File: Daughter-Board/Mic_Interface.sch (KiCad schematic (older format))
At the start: 11 parts, among them J301 Conn_01x08_0.5mm_Female_Kyoce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, U102 LM324A, U105 74HC4016, U107 MC74VHCT126A, U108 74HC4016

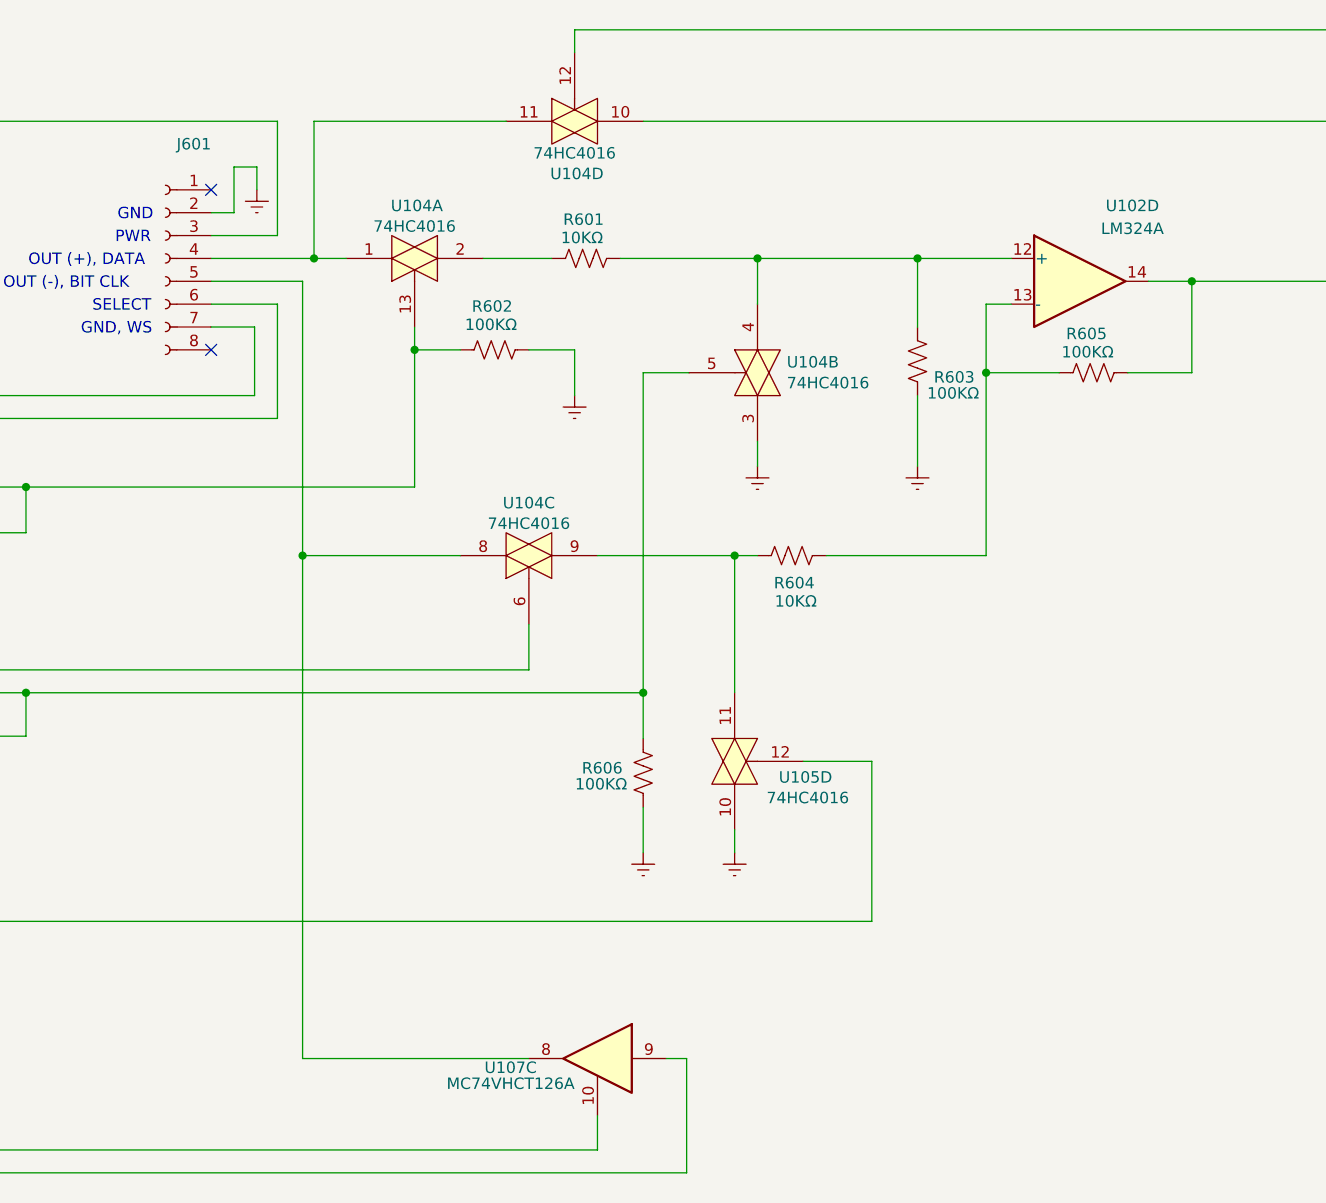
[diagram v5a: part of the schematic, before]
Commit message: Add connector for PICkit to MCU interface.
In the process of adding the PICkit connector some control lines had to be moved.
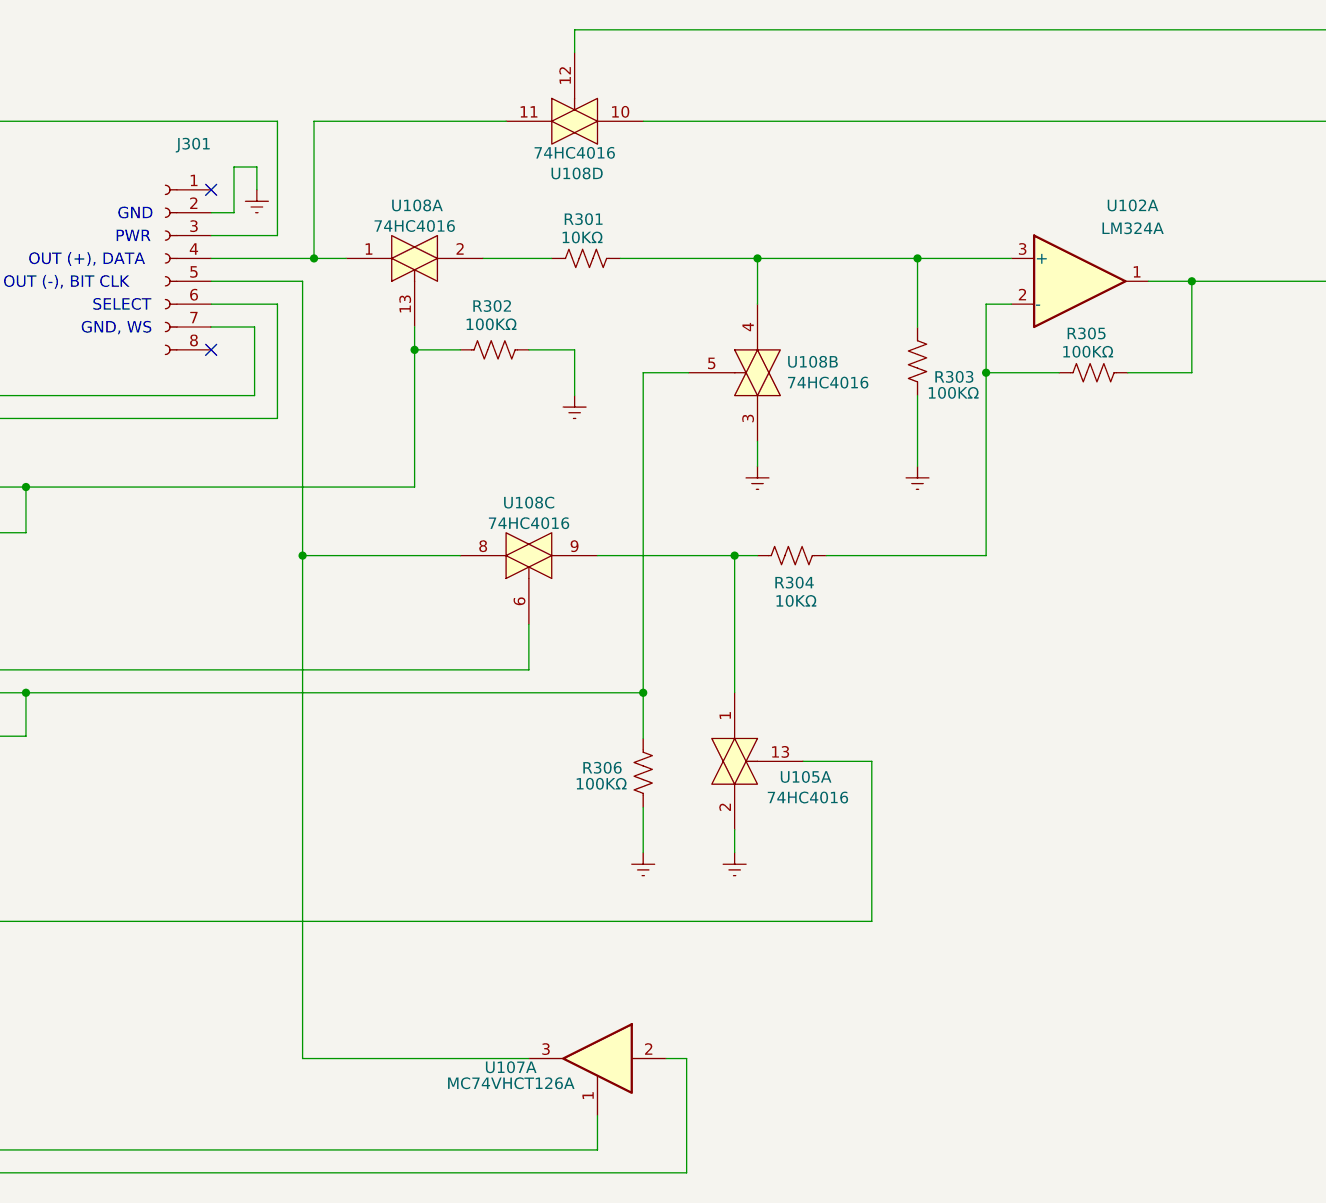
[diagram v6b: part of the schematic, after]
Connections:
- net AOut: now also U102.1; no longer U102.14
- net CLK_EN: now also U107.1; no longer U107.10
- net GNDREF: now also U105.2; no longer U105.10
- net MST_CLK: now also U107.2; no longer U107.9
- net SingleGain: now also U105.13; no longer U105.12
- net at R301.1, R303.2, U108.4: now also U102.3 (+); no longer U102.12 (+)
- net at R304.2, R305.2: now also U102.2 (-); no longer U102.13 (-)
- net at R304.1, U108.9: now also U105.1; no longer U105.11
- net at J301.5 (Pin_5), U108.8: now also U107.3; no longer U107.8
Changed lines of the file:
@@
 $Descr A4 11693 8268
 encoding utf-8
-Sheet 6 6
+Sheet 3 6
 Title "Daughter Board"
 Date ""
@@
 AR Path="/6159E578/612F28D7" Ref="R601"  Part="1"
 AR Path="/6159EF26/612F28D7" Ref="R501"  Part="1"
-F 0 "R601" V 6080 1900 50  0000 L CNN
+F 0 "R301" V 6080 1900 50  0000 L CNN
 F 1 "10KΩ" V 6160 1890 50  0000 L CNN
 F 2 "Resistor_SMD:R_1206_3216Metric" V 6290 1990 50  0001 C CNN
@@
 AR Path="/6159E578/612F28DD" Ref="R603"  Part="1"
 AR Path="/6159EF26/612F28DD" Ref="R503"  Part="1"
-F 0 "R603" H 7450 2520 50  0000 L CNN
+F 0 "R303" H 7450 2520 50  0000 L CNN
 F 1 "100KΩ" H 7430 2590 50  0000 L CNN
 F 2 "Resistor_SMD:R_1206_3216Metric" V 7740 2440 50  0001 C CNN
@@
 $Comp
 L Amplifier_Operational:LM324A U?
-U 4 1 612F28EA
+U 1 1 612F28EA
 P 8410 2100
 AR Path="/612F28EA" Ref="U?"  Part="1"
@@
 F 2 "Package_SO:SOIC-14_3.9x8.7mm_P1.27mm" H 8360 2200 50  0001 C CNN
 F 3 "" H 8460 2300 50  0001 C CNN
-	4    8410 2100
+	1    8410 2100
 	1    0    0    -1
 $EndComp
@@
 AR Path="/6159E578/612F28F6" Ref="R605"  Part="1"
 AR Path="/6159EF26/612F28F6" Ref="R505"  Part="1"
-F 0 "R605" V 8300 2380 50  0000 L CNN
+F 0 "R305" V 8300 2380 50  0000 L CNN
 F 1 "100KΩ" V 8380 2360 50  0000 L CNN
 F 2 "Resistor_SMD:R_1206_3216Metric" V 8510 2490 50  0001 C CNN
@@
 AR Path="/6159E578/612F2915" Ref="R604"  Part="1"
 AR Path="/6159EF26/612F2915" Ref="R504"  Part="1"
-F 0 "R604" V 7030 3200 50  0000 L CNN
+F 0 "R304" V 7030 3200 50  0000 L CNN
 F 1 "10KΩ" V 6950 3190 50  0000 L CNN
 F 2 "Resistor_SMD:R_1206_3216Metric" V 7190 3290 50  0001 C CNN
@@
 $Comp
 L 74xx:74LS126 U?
-U 3 1 612F29C2
+U 1 1 612F29C2
 P 6300 5500
 AR Path="/60E235BF/612F29C2" Ref="U?"  Part="1"
@@
 F 3 "" H 6300 5500 50  0001 C CNN
 F 4 "771-74VHCT126D118" H 6300 5500 50  0001 C CNN "Mouser #"
-	3    6300 5500
+	1    6300 5500
 	-1   0    0    -1
 $EndComp
@@
 AR Path="/6159E578/6151F074" Ref="R606"  Part="1"
 AR Path="/6159EF26/6151F074" Ref="R506"  Part="1"
-F 0 "R606" H 6590 4230 50  0000 L CNN
+F 0 "R306" H 6590 4230 50  0000 L CNN
 F 1 "100KΩ" H 6570 4300 50  0000 L CNN
 F 2 "Resistor_SMD:R_1206_3216Metric" V 6540 4240 50  0001 C CNN
@@
 AR Path="/6159E578/61527AC0" Ref="R602"  Part="1"
 AR Path="/6159EF26/61527AC0" Ref="R502"  Part="1"
-F 0 "R602" V 5660 2300 50  0000 L CNN
+F 0 "R302" V 5660 2300 50  0000 L CNN
 F 1 "100KΩ" V 5740 2270 50  0000 L CNN
 F 2 "Resistor_SMD:R_1206_3216Metric" V 5890 2390 50  0001 C CNN
@@
 AR Path="/6159E578/612F293F" Ref="J601"  Part="1"
 AR Path="/6159EF26/612F293F" Ref="J501"  Part="1"
-F 0 "J601" H 4210 2600 50  0000 L CNN
+F 0 "J301" H 4210 2600 50  0000 L CNN
 F 1 "Conn_01x08_0.5mm_Female_Kyocera" H 3650 1570 50  0001 L CNN
 F 2 "dcm-footprint:Kyocera_6288" H 4410 2100 50  0001 C CNN
@@
 AR Path="/6159EF26/615B1C2B" Ref="U103"  Part="1"
 AR Path="/6159E578/615B1C2B" Ref="U104"  Part="1"
-F 0 "U104" H 5510 1770 50  0000 C CNN
+F 0 "U108" H 5510 1770 50  0000 C CNN
 F 1 "74HC4016" H 5500 1860 50  0000 C CNN
 F 2 "" H 5500 2000 50  0001 C CNN
@@
 AR Path="/6159EF26/615B2703" Ref="U103"  Part="2"
 AR Path="/6159E578/615B2703" Ref="U104"  Part="2"
-F 0 "U104" V 6954 2372 50  0000 R CNN
+F 0 "U108" V 6954 2372 50  0000 R CNN
 F 1 "74HC4016" V 7045 2372 50  0000 R CNN
 F 2 "" H 7000 2500 50  0001 C CNN
@@
 AR Path="/6159EF26/615B41E1" Ref="U103"  Part="3"
 AR Path="/6159E578/615B41E1" Ref="U104"  Part="3"
-F 0 "U104" H 6000 3070 50  0000 C CNN
+F 0 "U108" H 6000 3070 50  0000 C CNN
 F 1 "74HC4016" H 6000 3160 50  0000 C CNN
 F 2 "" H 6000 3300 50  0001 C CNN
@@
 $Comp
 L 4xxx:4016 U105
-U 4 1 615B5217
+U 1 1 615B5217
 P 6900 4200
 AR Path="/612D7BBA/615B5217" Ref="U105"  Part="1"
@@
 F 2 "" H 6900 4200 50  0001 C CNN
 F 3 "http://www.ti.com/lit/ds/symlink/cd4016b.pdf" H 6900 4200 50  0001 C CNN
-	4    6900 4200
+	1    6900 4200
 	0    1    1    0
 $EndComp
@@
 AR Path="/6159EF26/615D07EE" Ref="U103"  Part="4"
 AR Path="/6159E578/615D07EE" Ref="U104"  Part="4"
-F 0 "U104" H 6210 1170 50  0000 C CNN
+F 0 "U108" H 6210 1170 50  0000 C CNN
 F 1 "74HC4016" H 6200 1260 50  0000 C CNN
 F 2 "" H 6200 1400 50  0001 C CNN

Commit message: Modify schematic to recover PCB layout.
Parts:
- R301, R302, R303, R304, R305, R306: footprint Resistor_SMD:R_1206_3216Metric -> Resistor_SMD:R_0805_2012Metric
- U102: footprint Package_SO:SOIC-14_3.9x8.7mm_P1.27mm -> Package_SO:TSSOP-14_4.4x5mm_P0.65mm
- U105, U108: footprint (none) -> Package_SO:SOIC-14_3.9x8.7mm_P1.27mm
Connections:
- net MST_CLK renamed MIC_MST_CLK
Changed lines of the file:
@@
 F 0 "R301" V 6080 1900 50  0000 L CNN
 F 1 "10KΩ" V 6160 1890 50  0000 L CNN
-F 2 "Resistor_SMD:R_1206_3216Metric" V 6290 1990 50  0001 C CNN
+F 2 "Resistor_SMD:R_0805_2012Metric" V 6290 1990 50  0001 C CNN
 F 3 "~" H 6250 2000 50  0001 C CNN
 F 4 "541-3983-1-ND" V 6250 2000 50  0001 C CNN "DigiKey #"
@@
 F 0 "R303" H 7450 2520 50  0000 L CNN
 F 1 "100KΩ" H 7430 2590 50  0000 L CNN
-F 2 "Resistor_SMD:R_1206_3216Metric" V 7740 2440 50  0001 C CNN
+F 2 "Resistor_SMD:R_0805_2012Metric" V 7740 2440 50  0001 C CNN
 F 3 "~" H 7700 2450 50  0001 C CNN
 F 4 "541-4173-1-ND" H 7700 2450 50  0001 C CNN "DigiKey #"
@@
 F 0 "U102" H 8640 2430 50  0000 C CNN
 F 1 "LM324A" H 8640 2330 50  0000 C CNN
-F 2 "Package_SO:SOIC-14_3.9x8.7mm_P1.27mm" H 8360 2200 50  0001 C CNN
+F 2 "Package_SO:TSSOP-14_4.4x5mm_P0.65mm" H 8360 2200 50  0001 C CNN
 F 3 "" H 8460 2300 50  0001 C CNN
 	1    8410 2100
@@
 F 0 "R305" V 8300 2380 50  0000 L CNN
 F 1 "100KΩ" V 8380 2360 50  0000 L CNN
-F 2 "Resistor_SMD:R_1206_3216Metric" V 8510 2490 50  0001 C CNN
+F 2 "Resistor_SMD:R_0805_2012Metric" V 8510 2490 50  0001 C CNN
 F 3 "~" H 8470 2500 50  0001 C CNN
 F 4 "541-4173-1-ND" V 8470 2500 50  0001 C CNN "DigiKey #"
@@
 F 0 "R304" V 7030 3200 50  0000 L CNN
 F 1 "10KΩ" V 6950 3190 50  0000 L CNN
-F 2 "Resistor_SMD:R_1206_3216Metric" V 7190 3290 50  0001 C CNN
+F 2 "Resistor_SMD:R_0805_2012Metric" V 7190 3290 50  0001 C CNN
 F 3 "~" H 7150 3300 50  0001 C CNN
 F 4 "541-3983-1-ND" V 7150 3300 50  0001 C CNN "DigiKey #"
@@
 	4900 1400 3210 1400
 Text HLabel 3210 6000 0    50   Input ~ 0
-MST_CLK
+MIC_MST_CLK
 Wire Wire Line
 	6600 5500 6690 5500
@@
 F 0 "R306" H 6590 4230 50  0000 L CNN
 F 1 "100KΩ" H 6570 4300 50  0000 L CNN
-F 2 "Resistor_SMD:R_1206_3216Metric" V 6540 4240 50  0001 C CNN
+F 2 "Resistor_SMD:R_0805_2012Metric" V 6540 4240 50  0001 C CNN
 F 3 "~" H 6500 4250 50  0001 C CNN
 	1    6500 4250
@@
 F 0 "R302" V 5660 2300 50  0000 L CNN
 F 1 "100KΩ" V 5740 2270 50  0000 L CNN
-F 2 "Resistor_SMD:R_1206_3216Metric" V 5890 2390 50  0001 C CNN
+F 2 "Resistor_SMD:R_0805_2012Metric" V 5890 2390 50  0001 C CNN
 F 3 "~" H 5850 2400 50  0001 C CNN
 F 4 "5414173-1-ND" V 5850 2400 50  0001 C CNN "DigiKey #"
@@
 F 0 "U108" H 5510 1770 50  0000 C CNN
 F 1 "74HC4016" H 5500 1860 50  0000 C CNN
-F 2 "" H 5500 2000 50  0001 C CNN
+F 2 "Package_SO:SOIC-14_3.9x8.7mm_P1.27mm" H 5500 2000 50  0001 C CNN
 F 3 "http://www.ti.com/lit/ds/symlink/cd4016b.pdf" H 5500 2000 50  0001 C CNN
 	1    5500 2000
@@
 F 0 "U108" V 6954 2372 50  0000 R CNN
 F 1 "74HC4016" V 7045 2372 50  0000 R CNN
-F 2 "" H 7000 2500 50  0001 C CNN
+F 2 "Package_SO:SOIC-14_3.9x8.7mm_P1.27mm" H 7000 2500 50  0001 C CNN
 F 3 "http://www.ti.com/lit/ds/symlink/cd4016b.pdf" H 7000 2500 50  0001 C CNN
 	2    7000 2500
@@
 F 0 "U108" H 6000 3070 50  0000 C CNN
 F 1 "74HC4016" H 6000 3160 50  0000 C CNN
-F 2 "" H 6000 3300 50  0001 C CNN
+F 2 "Package_SO:SOIC-14_3.9x8.7mm_P1.27mm" H 6000 3300 50  0001 C CNN
 F 3 "http://www.ti.com/lit/ds/symlink/cd4016b.pdf" H 6000 3300 50  0001 C CNN
 	3    6000 3300
@@
 F 0 "U105" V 6970 4510 50  0000 C CNN
 F 1 "74HC4016" V 7060 4520 50  0000 C CNN
-F 2 "" H 6900 4200 50  0001 C CNN
+F 2 "Package_SO:SOIC-14_3.9x8.7mm_P1.27mm" H 6900 4200 50  0001 C CNN
 F 3 "http://www.ti.com/lit/ds/symlink/cd4016b.pdf" H 6900 4200 50  0001 C CNN
 	1    6900 4200
@@
 F 0 "U108" H 6210 1170 50  0000 C CNN
 F 1 "74HC4016" H 6200 1260 50  0000 C CNN
-F 2 "" H 6200 1400 50  0001 C CNN
+F 2 "Package_SO:SOIC-14_3.9x8.7mm_P1.27mm" H 6200 1400 50  0001 C CNN
 F 3 "http://www.ti.com/lit/ds/symlink/cd4016b.pdf" H 6200 1400 50  0001 C CNN
 	4    6200 1400
